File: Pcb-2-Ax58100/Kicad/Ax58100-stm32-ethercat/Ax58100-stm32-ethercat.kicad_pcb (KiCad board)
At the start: 4 copper layers, 94.5 x 59.2 mm, 131 parts, among them J1 Conn_01x02_Pin, J10 DAC1, J11 Encoder 1, J12 Encoder 2, J13 Encoder 3, J14 Encoder 4, J2 STLINK, J3 Conn_01x06_Pin, J4 Conn_01x06_Pin, J5 Conn_01x06_Pin, J6 Serial usart1, J7 Stepper 1, J8 Stepper 2, J9 I2C bus2, SW1 SW PB, U1 AX58100, U2 24LC32A, U3 AMS1117-1.2, U4 AMS1117-3.3, U5 STM32F407VGT6, Y1 NXK25.000AE12F-KAB6-12, Y2 8 MHz

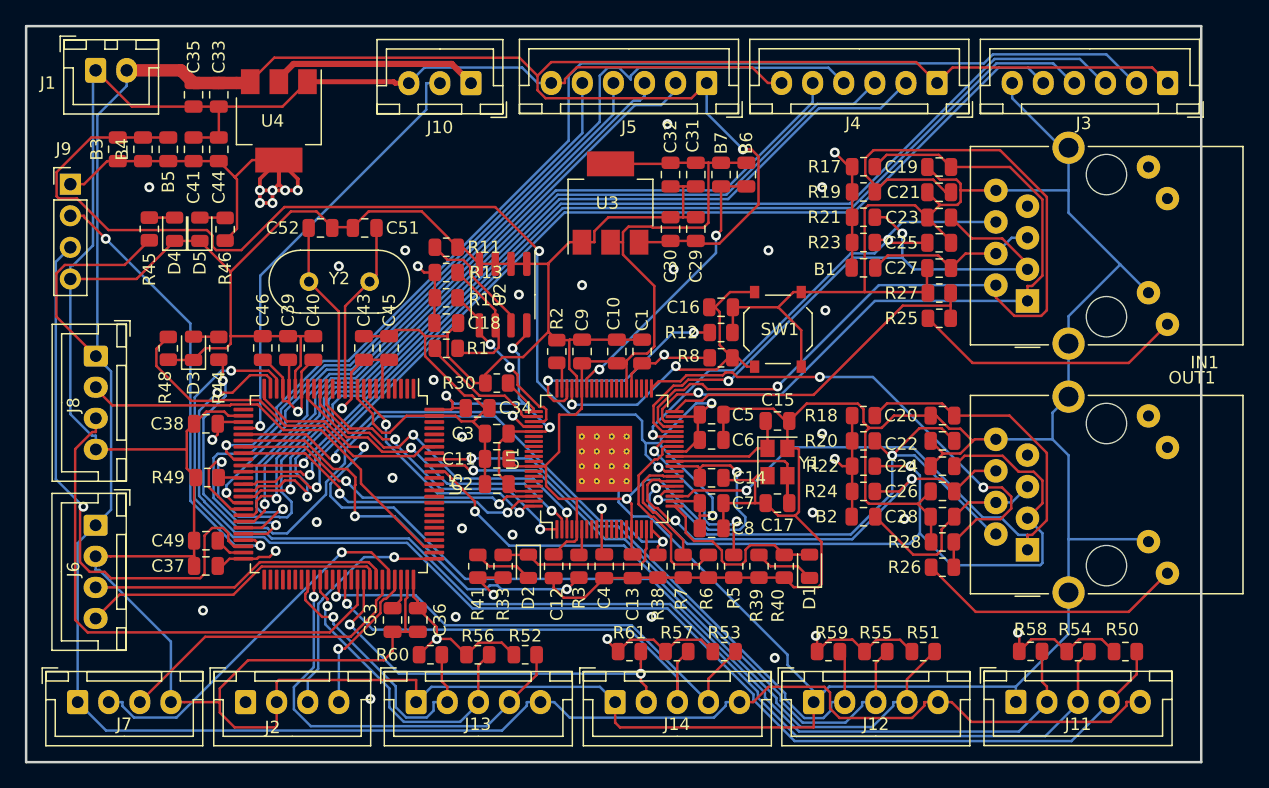
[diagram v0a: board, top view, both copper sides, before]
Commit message: Geographic annotation on pcb 2
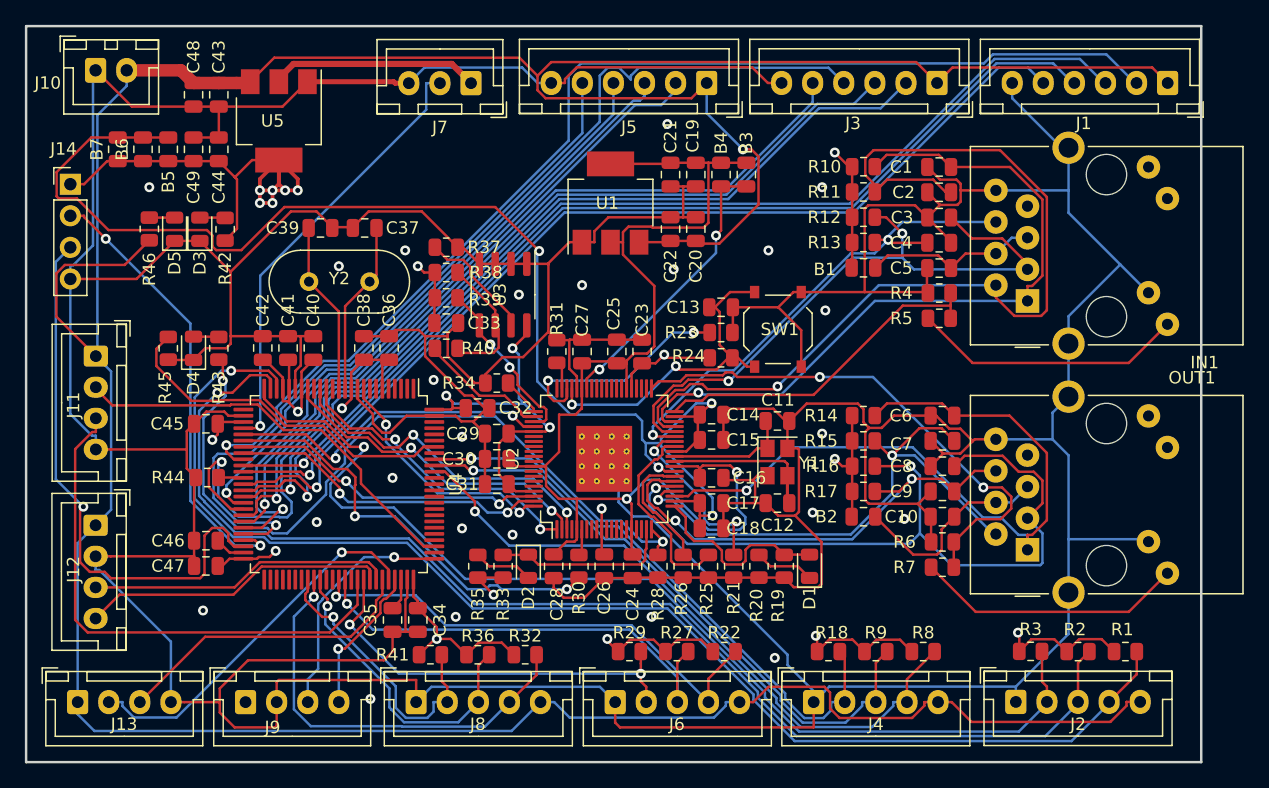
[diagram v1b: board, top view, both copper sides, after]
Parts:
- renumbered B6 to B3, B7 to B4, B4 to B6, B3 to B7, C19 to C1, C28 to C10, C15 to C11, C17 to C12, C16 to C13, C5 to C14, C6 to C15, C14 to C16, C7 to C17, C8 to C18, C31 to C19, C21 to C2, C29 to C20, C32 to C21, C30 to C22, C1 to C23, C13 to C24, C10 to C25, C4 to C26, C9 to C27, C12 to C28, C3 to C29, C23 to C3, C11 to C30, C2 to C31, C34 to C32, C18 to C33, C36 to C34, C53 to C35, C45 to C36, C51 to C37, C43 to C38, C52 to C39, C25 to C4, C39 to C41, C46 to C42, C33 to C43, C38 to C45, C49 to C46, C37 to C47, C35 to C48, C41 to C49, C27 to C5, C20 to C6, C22 to C7, C24 to C8, C26 to C9, D5 to D3, D3 to D4, D4 to D5, J3 to J1, J1 to J10, J8 to J11, J6 to J12, J7 to J13, J9 to J14, J11 to J2, J4 to J3, J12 to J4, J14 to J6, J10 to J7, J13 to J8, J2 to J9, R50 to R1, R17 to R10, R19 to R11, R21 to R12, R23 to R13, R18 to R14, R20 to R15, R22 to R16, R24 to R17, R59 to R18, R40 to R19, R54 to R2, R39 to R20, R5 to R21, R53 to R22, R12 to R23, R8 to R24, R6 to R25, R7 to R26, R57 to R27, R38 to R28, R61 to R29, R58 to R3, R3 to R30, R2 to R31, R52 to R32, R30 to R34, R41 to R35, R56 to R36, R11 to R37, R13 to R38, R10 to R39, R27 to R4, R1 to R40, R60 to R41, R46 to R42, R44 to R43, R49 to R44, R48 to R45, R45 to R46, R25 to R5, R28 to R6, R26 to R7, R51 to R8, R55 to R9, U3 to U1, U1 to U2, U2 to U3, U5 to U4, U4 to U5
